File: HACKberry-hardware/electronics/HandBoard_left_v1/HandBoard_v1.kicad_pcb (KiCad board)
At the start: 2 copper layers, 60.8 x 54.8 mm, 12 parts, among them CON1 BARREL_JACK, SW1:MAX1 SW_PUSH_SKRGAQD010, SW2:MIN1 SW_PUSH_SKRGAQD010, SW3:Thumb1 SW_PUSH_SKRGAQD010, SW4:Middle1 SW_PUSH_SKRGAQD010, SW5 SWITCH_SS-12SDP2, U1 3-CONDUCTOR_MINIATUIRE_JACK_M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, U2 Arduino_Micro, U3 Seed_Studio_Adjustable_DC/DC_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, U4 Servo_Motor_S03N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

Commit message: Update HandBoard garber data for left hand
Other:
- board text added: "HandBoard_v1_Left"
- board text removed: "HandBoard_v1"
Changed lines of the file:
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@@
     (links 23)
     (no_connects 1)
-    (area 96.561099 85.319599 157.461101 140.209601)
+    (area 95.3061 68.711552 159.4021 154.678413)
     (thickness 1.6)
     (drawings 55)
@@
   )
   (setup
-    (last_trace_width 1)
+    (last_trace_width 0.5)
     (user_trace_width 0.5)
     (user_trace_width 1)
@@
       (drillshape 0)
       (scaleselection 1)
-      (outputdirectory 160111HandBoard_v1_2/))
+      (outputdirectory 160229HandBoard_v1_2/))
   )
   (net 0 "")
@@
     )
   )
-  (gr_text HandBoard_v1 (at 129.9591 148.4376) (layer F.SilkS)
-    (effects (font (size 1.5 1.5) (thickness 0.3)) (justify left))
-  )
-  (gr_text IN- (at 193.5551 88.8376) (layer F.SilkS)
-    (effects (font (size 1.5 1.5) (thickness 0.3)) (justify left))
-  )
-  (gr_text PWM (at 129.9591 69.6976) (layer F.SilkS)
-    (effects (font (size 1.5 1.5) (thickness 0.3)) (justify left))
-  )
-  (gr_text V+ (at 124.4411 68.1736) (layer F.SilkS)
-    (effects (font (size 1.5 1.5) (thickness 0.3)) (justify left))
-  )
-  (gr_text GND (at 125.3871 65.6336) (layer F.SilkS)
-    (effects (font (size 1.5 1.5) (thickness 0.3)) (justify left))
-  )
-  (gr_text IN+ (at 193.5551 81.2376) (layer F.SilkS)
-    (effects (font (size 1.5 1.5) (thickness 0.3)) (justify left))
-  )
-  (gr_line (start 189.3051 88.8376) (end 187.7051 87.2376) (angle 90) (layer F.SilkS) (width 0.1))
-  (gr_line (start 193.5551 88.8376) (end 189.3051 88.8376) (angle 90) (layer F.SilkS) (width 0.1))
-  (gr_line (start 189.2551 81.2376) (end 187.7051 82.7876) (angle 90) (layer F.SilkS) (width 0.1))
-  (gr_line (start 193.5551 81.2376) (end 189.2551 81.2376) (angle 90) (layer F.SilkS) (width 0.1))
-  (gr_text OUT- (at 193.5551 86.2876) (layer F.SilkS)
-    (effects (font (size 1.5 1.5) (thickness 0.3)) (justify left))
-  )
-  (gr_text OUT+ (at 193.5551 83.7376) (layer F.SilkS)
-    (effects (font (size 1.5 1.5) (thickness 0.3)) (justify left))
-  )
-  (gr_line (start 190.5551 86.2876) (end 193.5551 86.2876) (angle 90) (layer F.SilkS) (width 0.1))
-  (gr_line (start 190.5551 83.7376) (end 193.5551 83.7376) (angle 90) (layer F.SilkS) (width 0.1))
-  (gr_text Index (at 73.5531 67.8336 90) (layer F.SilkS)
+  (gr_line (start 124.1211 127.6336) (end 124.1211 121.7836) (angle 90) (layer F.SilkS) (width 0.1))
+  (gr_line (start 120.0711 131.6836) (end 124.1211 127.6336) (angle 90) (layer F.SilkS) (width 0.1))
+  (gr_line (start 120.7711 127.9836) (end 120.7711 121.8836) (angle 90) (layer F.SilkS) (width 0.1))
+  (gr_line (start 117.0211 131.7336) (end 120.7711 127.9836) (angle 90) (layer F.SilkS) (width 0.1))
+  (gr_line (start 117.1711 128.5336) (end 113.9711 131.7336) (angle 90) (layer F.SilkS) (width 0.1))
+  (gr_line (start 117.1711 122.0336) (end 117.1711 128.5336) (angle 90) (layer F.SilkS) (width 0.1))
+  (gr_text HandBoard_v1_Left (at 97.3211 108.3336) (layer F.SilkS)
+    (effects (font (size 1.5 1.5) (thickness 0.3)) (justify left))
+  )
+  (gr_text IN- (at 139.8051 133.8876) (layer F.SilkS)
+    (effects (font (size 1.5 1.5) (thickness 0.3)) (justify left))
+  )
+  (gr_text PWM (at 121.9711 133.4836) (layer F.SilkS)
+    (effects (font (size 1.5 1.5) (thickness 0.3)) (justify left))
+  )
+  (gr_text V+ (at 122.0711 136.1336) (layer F.SilkS)
+    (effects (font (size 1.5 1.5) (thickness 0.3)) (justify left))
+  )
+  (gr_text GND (at 121.9711 138.5836) (layer F.SilkS)
+    (effects (font (size 1.5 1.5) (thickness 0.3)) (justify left))
+  )
+  (gr_text IN+ (at 139.8051 126.2876) (layer F.SilkS)
+    (effects (font (size 1.5 1.5) (thickness 0.3)) (justify left))
+  )
+  (gr_line (start 150.6871 126.3296) (end 152.2871 127.9296) (angle 90) (layer F.SilkS) (width 0.1))
+  (gr_line (start 146.4371 126.3296) (end 150.6871 126.3296) (angle 90) (layer F.SilkS) (width 0.1))
+  (gr_line (start 150.7371 133.9296) (end 152.2871 132.3796) (angle 90) (layer F.SilkS) (width 0.1))
+  (gr_line (start 146.4371 133.9296) (end 150.7371 133.9296) (angle 90) (layer F.SilkS) (width 0.1))
+  (gr_text OUT- (at 139.8051 131.3376) (layer F.SilkS)
+    (effects (font (size 1.5 1.5) (thickness 0.3)) (justify left))
+  )
+  (gr_text OUT+ (at 139.8051 128.7876) (layer F.SilkS)
+    (effects (font (size 1.5 1.5) (thickness 0.3)) (justify left))
+  )
+  (gr_line (start 149.4371 128.8796) (end 146.4371 128.8796) (angle 90) (layer F.SilkS) (width 0.1))
+  (gr_line (start 149.4371 131.4296) (end 146.4371 131.4296) (angle 90) (layer F.SilkS) (width 0.1))
+  (gr_text Index (at 124.2211 115.7836 90) (layer F.SilkS)
     (effects (font (size 1.5 1.5) (thickness 0.3)) (justify right))
   )
-  (gr_text Middle (at 70.3531 67.8336 90) (layer F.SilkS)
+  (gr_text Middle (at 120.9211 114.5336 90) (layer F.SilkS)
     (effects (font (size 1.5 1.5) (thickness 0.3)) (justify right))
   )
-  (gr_text Thumb (at 66.7131 69.4436 90) (layer F.SilkS)
+  (gr_text Thumb (at 117.2631 114.3936 90) (layer F.SilkS)
     (effects (font (size 1.5 1.5) (thickness 0.3)) (justify right))
   )
-  (gr_line (start 73.5531 66.3336) (end 73.5531 67.8336) (angle 90) (layer F.SilkS) (width 0.1))
-  (gr_line (start 70.3531 66.3336) (end 70.3531 67.8336) (angle 90) (layer F.SilkS) (width 0.1))
-  (gr_line (start 70.5531 63.3336) (end 73.5531 66.3336) (angle 90) (layer F.SilkS) (width 0.1))
-  (gr_line (start 67.3531 63.3336) (end 70.3531 66.3336) (angle 90) (layer F.SilkS) (width 0.1))
-  (gr_line (start 67.1531 66.3336) (end 67.1531 67.8336) (angle 90) (layer F.SilkS) (width 0.1))
-  (gr_line (start 64.1531 63.3336) (end 67.1531 66.3336) (angle 90) (layer F.SilkS) (width 0.1))
   (gr_line (start 119.9411 91.4096) (end 119.9411 85.8696) (angle 90) (layer Edge.Cuts) (width 0.1))
   (gr_line (start 111.4411 85.3696) (end 119.4411 85.3696) (angle 90) (layer Edge.Cuts) (width 0.1))

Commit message: trial and error
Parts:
- moved U1 58.8 mm to (127.0, 150.2), turned to 0 degrees
- moved CON1 52.8 mm to (139.6, 147.5), turned to 0 degrees
- moved U2 40.2 mm to (127.0, 150.2), turned to 0 degrees
- moved U3 33.9 mm to (127.0, 150.2), turned to 0 degrees
- moved U5 21.2 mm to (127.0, 150.2)
- moved U6 19.5 mm to (127.0, 150.2)
- moved U4 18.1 mm to (127.0, 150.2)
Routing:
- net (no net): track 0.00 -> 377.9 mm, vias 0 -> 6
- net Net-(U2-Pad6): track 76.7 -> 0.00 mm
- net Net-(U2-Pad5): track 68.0 -> 0.00 mm
- net Net-(U3-Pad4): track 65.7 -> 0.00 mm, vias 2 -> 0
- net Net-(U2-Pad3): track 61.6 -> 0.00 mm, vias 4 -> 0
- net Net-(U3-Pad3): track 45.6 -> 0.00 mm
- net Net-(U1-Pad2): track 42.4 -> 0.00 mm
- net Net-(U1-Pad4): track 14.8 -> 0.00 mm
- net Net-(U2-PadNC): track 2.54 -> 0.00 mm

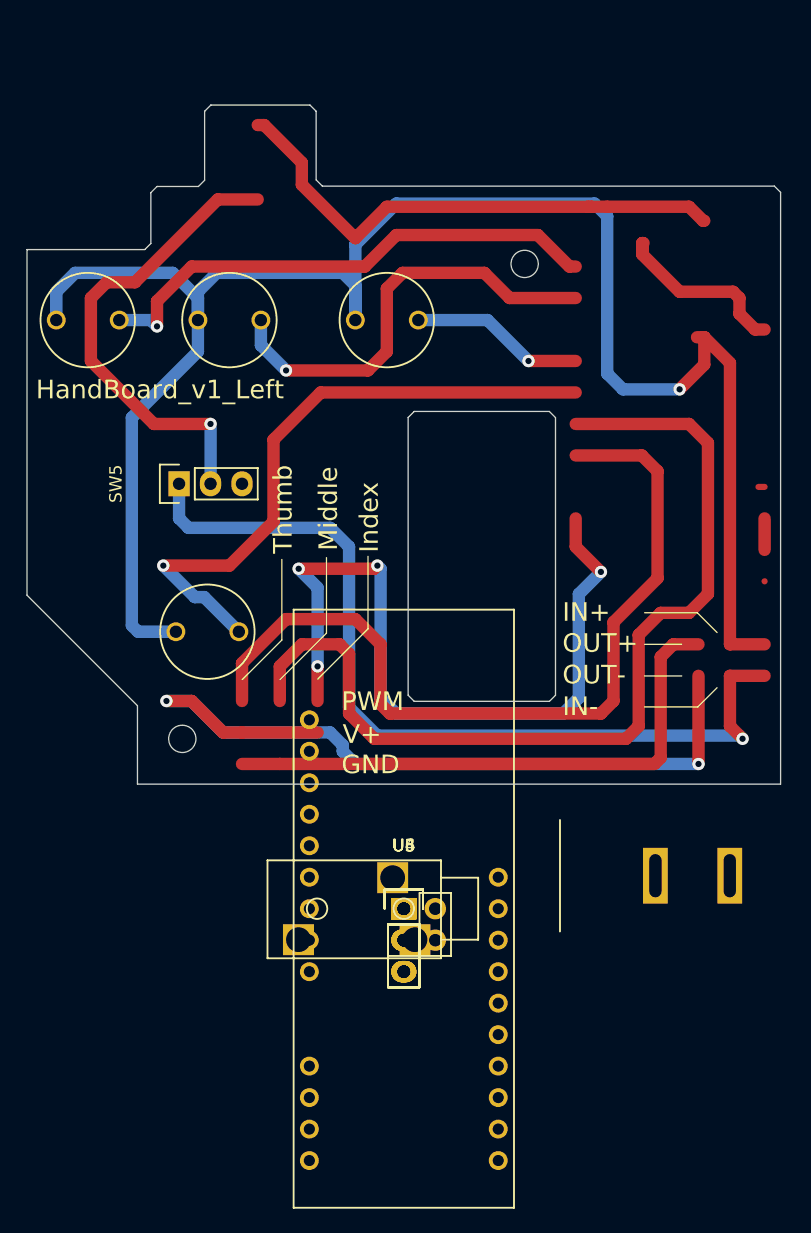
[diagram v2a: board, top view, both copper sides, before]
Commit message: change the arrangement of pins and the size of DC-DC converter and rewire all routes.
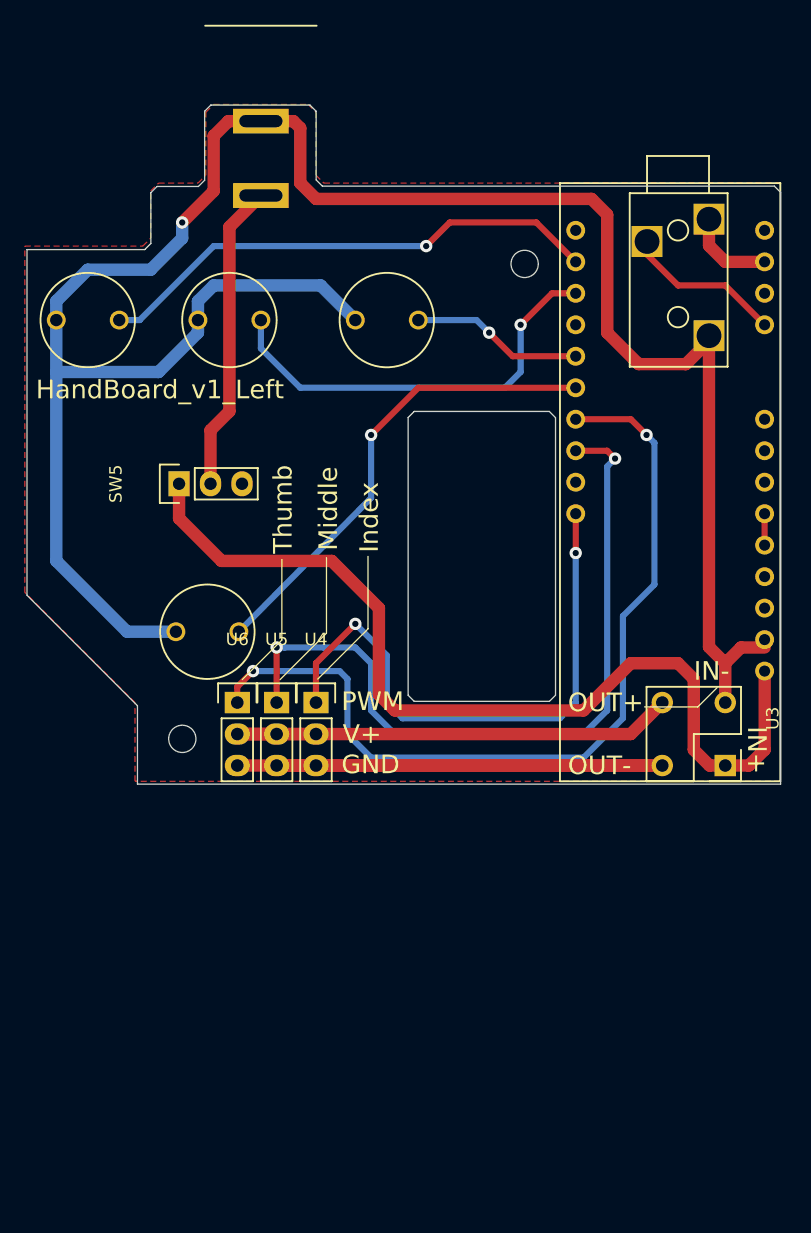
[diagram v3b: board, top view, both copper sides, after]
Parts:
- U3: footprint Pin_Headers:Pin_Header_Straight_2x02 -> HACKberry_v1:Pin_Header_Straight_2x02_Left_DCDC
- moved CON1 72.7 mm to (115.5, 79.0), turned to 270 degrees
- moved U1 59.0 mm to (149.1, 95.5), turned to 90 degrees
- moved U2 40.6 mm to (148.5, 115.8), turned to 180 degrees
- moved U3 29.1 mm to (151.7, 134.8), turned to 270 degrees
- moved U6 21.4 mm to (113.6, 133.6)
- moved U5 19.5 mm to (116.8, 133.6)
- moved U4 18.1 mm to (119.9, 133.6)
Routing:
- net (no net): track 377.9 -> 0.00 mm, vias 6 -> 0
- net Net-(U3-Pad3): track 0.00 -> 93.3 mm
- net Net-(U2-Pad6): track 0.00 -> 70.1 mm, vias 0 -> 2
- net Net-(U2-Pad5): track 0.00 -> 61.1 mm, vias 0 -> 2
- net Net-(U2-Pad3): track 0.00 -> 46.6 mm, vias 0 -> 2
- net Net-(U3-Pad4): track 0.00 -> 44.9 mm
- net Net-(CON1-Pad2): track 148.9 -> 178.0 mm
- net Net-(CON1-Pad1): track 38.4 -> 24.9 mm, vias 1 -> 0
- net /SW_PINCH: track 51.2 -> 38.3 mm
- net Net-(U1-Pad4): track 0.00 -> 12.9 mm
- net Net-(U1-Pad2): track 0.00 -> 7.16 mm
- net Net-(SW5-Pad1): track 71.6 -> 75.1 mm, vias 1 -> 0
- net Net-(U2-PadNC): track 0.00 -> 2.54 mm
- net /SW_OPEN: track 35.4 -> 34.4 mm
- net Net-(SW1:MAX1-Pad2): track 42.3 -> 41.4 mm
- added copper zone on F.Cu, net Net-(CON1-Pad2)

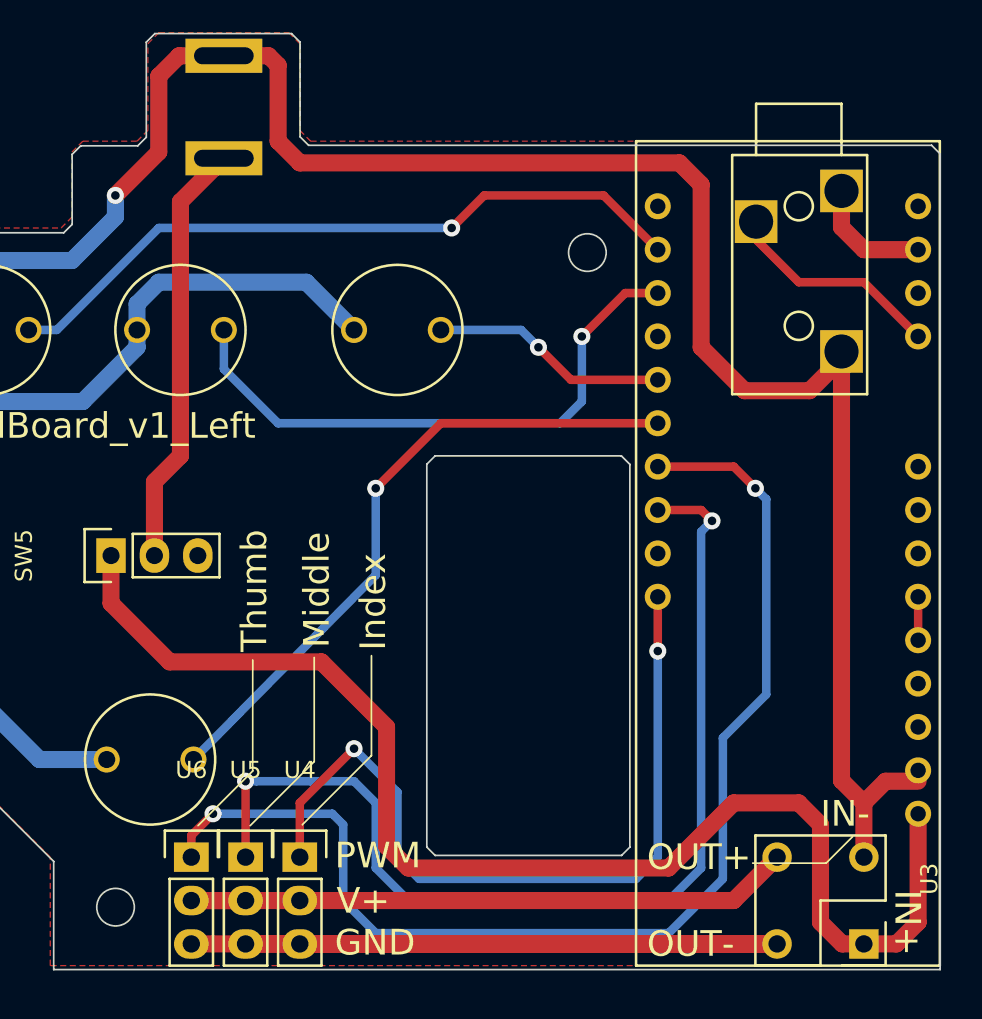
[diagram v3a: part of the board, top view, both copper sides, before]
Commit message: change the voltage to sensor to 5V
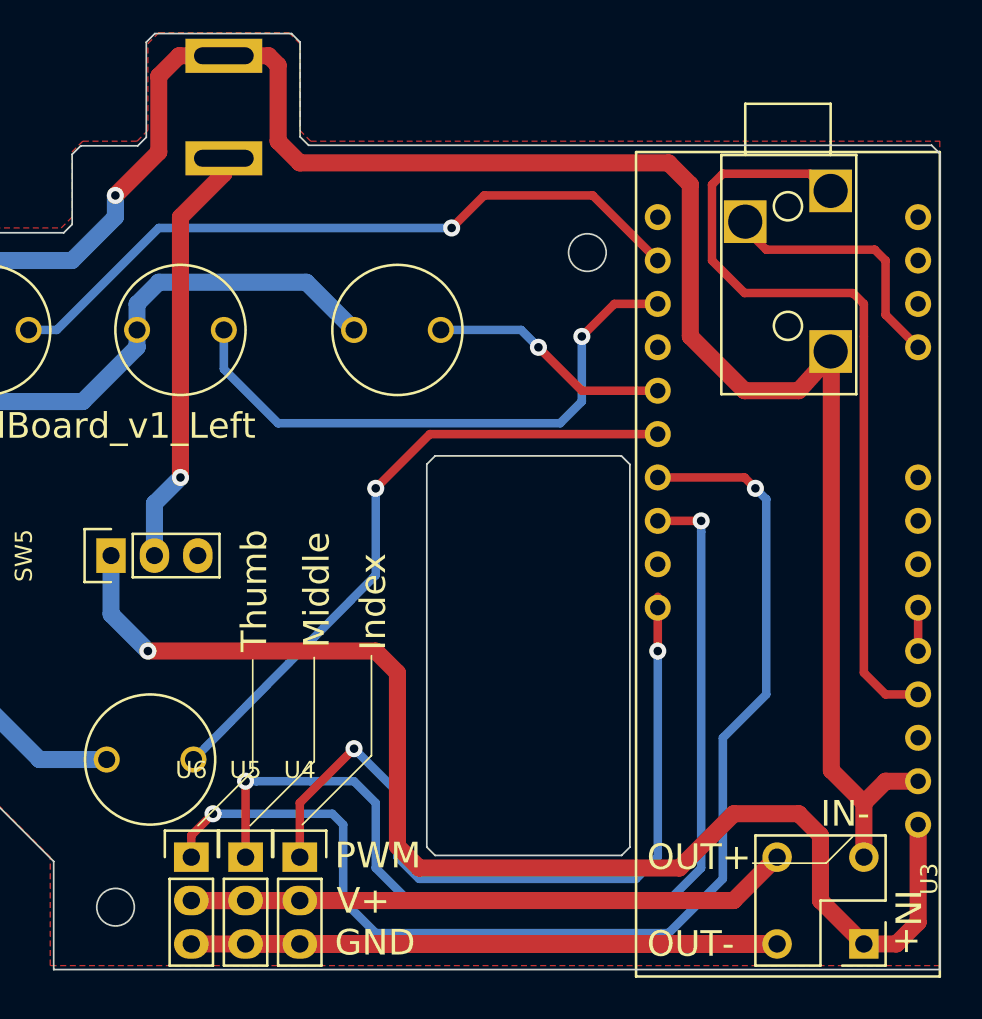
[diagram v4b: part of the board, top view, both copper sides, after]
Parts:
- moved U2 0.64 mm to (148.5, 116.4)
- moved U1 0.63 mm to (148.5, 95.5)
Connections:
- U2 pad 3V3: Net-(U1-Pad2) -> Net-(U2-Pad3V3)
- U2 pad 5V: Net-(U2-Pad5V) -> Net-(U1-Pad2)
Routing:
- net Net-(U1-Pad2): track 7.16 -> 47.9 mm
- net Net-(U1-Pad4): track 12.9 -> 15.3 mm
- net Net-(U2-Pad5): track 61.1 -> 59.9 mm
- net Net-(SW5-Pad1): track 75.1 -> 75.7 mm, vias 0 -> 1
- net Net-(CON1-Pad1): vias 0 -> 1
